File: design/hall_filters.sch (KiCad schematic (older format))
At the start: 11 parts

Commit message: Saved project with more recent version of KiCad. Added IRS2184 half bridge driver to BLDC_4_cache.lib
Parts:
- C4, C5, C6, C7: symbol C -> C-RESCUE-BLDC_4
- R10, R11, R12, R13, R7, R8, R9: symbol R -> R-RESCUE-BLDC_4
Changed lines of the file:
@@
 EESchema Schematic File Version 2
+LIBS:BLDC_4-rescue
 LIBS:power
 LIBS:device
@@
 LIBS:crf_1
 LIBS:BLDC_4-cache
-EELAYER 24 0
+EELAYER 25 0
 EELAYER END
 $Descr A4 11693 8268
@@
 $EndDescr
 $Comp
-L R R7
+L R-RESCUE-BLDC_4 R7
 U 1 1 53FBB581
 P 4900 3200
@@
 $EndComp
 $Comp
-L R R8
+L R-RESCUE-BLDC_4 R8
 U 1 1 53FBB588
 P 5550 3750
@@
 $EndComp
 $Comp
-L R R9
+L R-RESCUE-BLDC_4 R9
 U 1 1 53FBB58F
 P 5550 3650
@@
 $EndComp
 $Comp
-L R R10
+L R-RESCUE-BLDC_4 R10
 U 1 1 53FBB596
 P 5550 3550
@@
 $EndComp
 $Comp
-L C C5
+L C-RESCUE-BLDC_4 C5
 U 1 1 53FBB59D
 P 5950 4250
@@
 $EndComp
 $Comp
-L C C6
+L C-RESCUE-BLDC_4 C6
 U 1 1 53FBB5A4
 P 6200 4250
@@
 $EndComp
 $Comp
-L C C7
+L C-RESCUE-BLDC_4 C7
 U 1 1 53FBB5AB
 P 6450 4250
@@
 $EndComp
 $Comp
-L GND #PWR030
+L GND-RESCUE-BLDC_4 #PWR030
 U 1 1 53FBB5B2
 P 5950 4450
@@
 $EndComp
 $Comp
-L R R11
+L R-RESCUE-BLDC_4 R11
 U 1 1 53FBB5B8
 P 5000 3200
@@
 $EndComp
 $Comp
-L R R12
+L R-RESCUE-BLDC_4 R12
 U 1 1 53FBB5BF
 P 5100 3200
@@
 $EndComp
 $Comp
-L R R13
+L R-RESCUE-BLDC_4 R13
 U 1 1 53FBB5C6
 P 5200 3200
@@
 $EndComp
 $Comp
-L C C4
+L C-RESCUE-BLDC_4 C4
 U 1 1 53FBB5CD
 P 5100 4250
@@
 $EndComp
 $Comp
-L GND #PWR031
+L GND-RESCUE-BLDC_4 #PWR031
 U 1 1 53FBB5D4
 P 5100 4450
@@
 	5100 3850 5100 4050
 $Comp
-L GND #PWR033
+L GND-RESCUE-BLDC_4 #PWR033
 U 1 1 53FBB5F9
 P 6200 4450
@@
 $EndComp
 $Comp
-L GND #PWR034
+L GND-RESCUE-BLDC_4 #PWR034
 U 1 1 53FBB5FF
 P 6450 4450

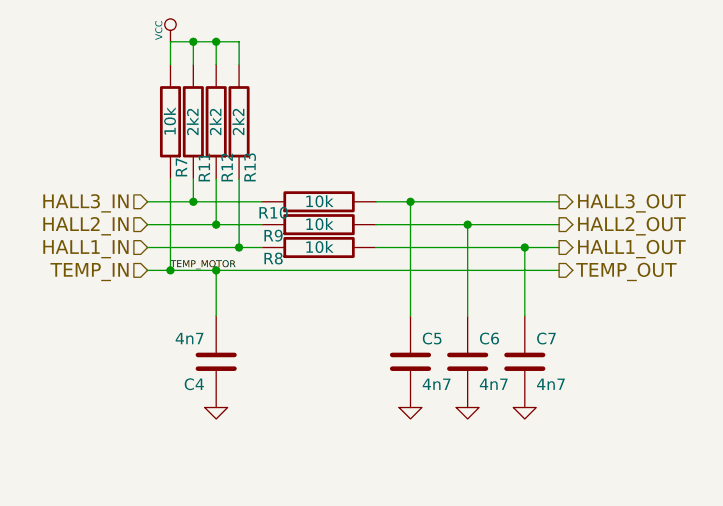
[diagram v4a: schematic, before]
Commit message: First complete draft of the schematics.
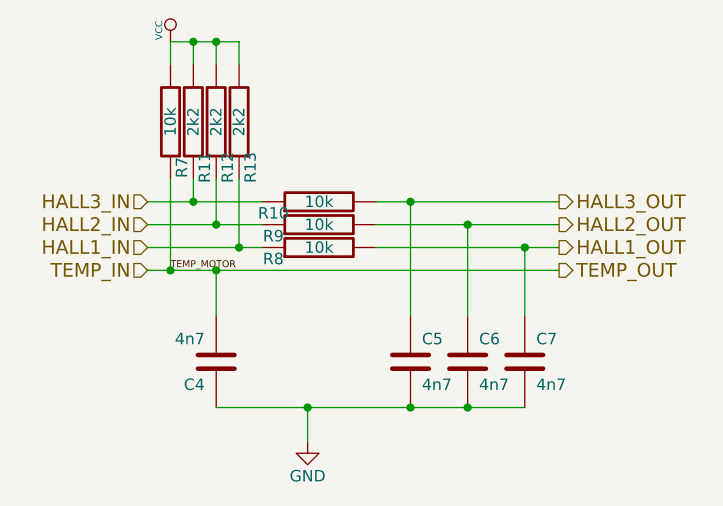
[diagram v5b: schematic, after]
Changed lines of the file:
@@
 $Descr A4 11693 8268
 encoding utf-8
-Sheet 4 10
+Sheet 4 11
 Title ""
-Date "25 Aug 2014"
+Date "2015-08-27"
 Rev ""
 Comp ""
@@
 $EndComp
 $Comp
-L GND-RESCUE-BLDC_4 #PWR030
-U 1 1 53FBB5B2
-P 5950 4450
-F 0 "#PWR030" H 5950 4450 30  0001 C CNN
-F 1 "GND" H 5950 4380 30  0001 C CNN
-F 2 "" H 5950 4450 60  0001 C CNN
-F 3 "" H 5950 4450 60  0001 C CNN
-	1    5950 4450
-	1    0    0    -1
-$EndComp
-$Comp
 L R-RESCUE-BLDC_4 R11
 U 1 1 53FBB5B8
@@
 $EndComp
 $Comp
-L GND-RESCUE-BLDC_4 #PWR031
-U 1 1 53FBB5D4
-P 5100 4450
-F 0 "#PWR031" H 5100 4450 30  0001 C CNN
-F 1 "GND" H 5100 4380 30  0001 C CNN
-F 2 "" H 5100 4450 60  0001 C CNN
-F 3 "" H 5100 4450 60  0001 C CNN
-	1    5100 4450
-	1    0    0    -1
-$EndComp
-$Comp
 L VCC #PWR032
 U 1 1 53FBB5DA
@@
 Wire Wire Line
 	5100 3850 5100 4050
-$Comp
-L GND-RESCUE-BLDC_4 #PWR033
-U 1 1 53FBB5F9
-P 6200 4450
-F 0 "#PWR033" H 6200 4450 30  0001 C CNN
-F 1 "GND" H 6200 4380 30  0001 C CNN
-F 2 "" H 6200 4450 60  0001 C CNN
-F 3 "" H 6200 4450 60  0001 C CNN
-	1    6200 4450
-	1    0    0    -1
-$EndComp
-$Comp
-L GND-RESCUE-BLDC_4 #PWR034
-U 1 1 53FBB5FF
-P 6450 4450
-F 0 "#PWR034" H 6450 4450 30  0001 C CNN
-F 1 "GND" H 6450 4380 30  0001 C CNN
-F 2 "" H 6450 4450 60  0001 C CNN
-F 3 "" H 6450 4450 60  0001 C CNN
-	1    6450 4450
-	1    0    0    -1
-$EndComp
 Text Label 4900 3850 0    30   ~ 0
 TEMP_MOTOR
@@
 Text HLabel 6600 3850 2    60   Output ~ 0
 TEMP_OUT
+$Comp
+L GND #PWR?
+U 1 1 55E74C47
+P 5500 4600
+F 0 "#PWR?" H 5500 4350 50  0001 C CNN
+F 1 "GND" H 5500 4450 50  0000 C CNN
+F 2 "" H 5500 4600 60  0000 C CNN
+F 3 "" H 5500 4600 60  0000 C CNN
+	1    5500 4600
+	1    0    0    -1
+$EndComp
+Wire Wire Line
+	5500 4600 5500 4450
+Wire Wire Line
+	5100 4450 6450 4450
+Connection ~ 5500 4450
+Connection ~ 5950 4450
+Connection ~ 6200 4450
 $EndSCHEMATC

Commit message: Assigned some footprints.
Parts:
- C4, C5, C6, C7: footprint SMD_Packages:SMD-0603_c -> Capacitors_SMD:C_0603
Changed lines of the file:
@@
 F 0 "C5" H 6000 4350 50  0000 L CNN
 F 1 "4n7" H 6000 4150 50  0000 L CNN
-F 2 "SMD_Packages:SMD-0603_c" H 5950 4250 60  0001 C CNN
+F 2 "Capacitors_SMD:C_0603" H 5950 4250 60  0001 C CNN
 F 3 "" H 5950 4250 60  0001 C CNN
 	1    5950 4250
@@
 F 0 "C6" H 6250 4350 50  0000 L CNN
 F 1 "4n7" H 6250 4150 50  0000 L CNN
-F 2 "SMD_Packages:SMD-0603_c" H 6200 4250 60  0001 C CNN
+F 2 "Capacitors_SMD:C_0603" H 6200 4250 60  0001 C CNN
 F 3 "" H 6200 4250 60  0001 C CNN
 	1    6200 4250
@@
 F 0 "C7" H 6500 4350 50  0000 L CNN
 F 1 "4n7" H 6500 4150 50  0000 L CNN
-F 2 "SMD_Packages:SMD-0603_c" H 6450 4250 60  0001 C CNN
+F 2 "Capacitors_SMD:C_0603" H 6450 4250 60  0001 C CNN
 F 3 "" H 6450 4250 60  0001 C CNN
 	1    6450 4250
@@
 F 0 "C4" H 5150 4350 50  0000 L CNN
 F 1 "4n7" H 5150 4150 50  0000 L CNN
-F 2 "SMD_Packages:SMD-0603_c" H 5100 4250 60  0001 C CNN
+F 2 "Capacitors_SMD:C_0603" H 5100 4250 60  0001 C CNN
 F 3 "" H 5100 4250 60  0001 C CNN
 	1    5100 4250
@@
 $EndComp
 $Comp
-L VCC #PWR032
+L VCC #PWR025
 U 1 1 53FBB5DA
 P 4900 2850
-F 0 "#PWR032" H 4900 2950 30  0001 C CNN
+F 0 "#PWR025" H 4900 2950 30  0001 C CNN
 F 1 "VCC" V 4850 2900 30  0000 C CNN
 F 2 "" H 4900 2850 60  0001 C CNN
@@
 TEMP_OUT
 $Comp
-L GND #PWR?
+L GND #PWR026
 U 1 1 55E74C47
 P 5500 4600
-F 0 "#PWR?" H 5500 4350 50  0001 C CNN
+F 0 "#PWR026" H 5500 4350 50  0001 C CNN
 F 1 "GND" H 5500 4450 50  0000 C CNN
 F 2 "" H 5500 4600 60  0000 C CNN

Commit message: Selected footprints
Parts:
- R10, R11, R12, R13, R7, R8, R9: footprint SMD_Packages:SMD-0603_r -> Resistors_SMD:R_0603
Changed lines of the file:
@@
 F 0 "R7" V 4850 3400 50  0000 C CNN
 F 1 "10k" V 4900 3200 50  0000 C CNN
-F 2 "SMD_Packages:SMD-0603_r" H 4900 3200 60  0001 C CNN
+F 2 "Resistors_SMD:R_0603" H 4900 3200 60  0001 C CNN
 F 3 "" H 4900 3200 60  0001 C CNN
 	1    4900 3200
@@
 F 0 "R8" V 5500 3950 50  0000 C CNN
 F 1 "10k" V 5550 3750 50  0000 C CNN
-F 2 "SMD_Packages:SMD-0603_r" H 5550 3750 60  0001 C CNN
+F 2 "Resistors_SMD:R_0603" H 5550 3750 60  0001 C CNN
 F 3 "" H 5550 3750 60  0001 C CNN
 	1    5550 3750
@@
 F 0 "R9" V 5500 3850 50  0000 C CNN
 F 1 "10k" V 5550 3650 50  0000 C CNN
-F 2 "SMD_Packages:SMD-0603_r" H 5550 3650 60  0001 C CNN
+F 2 "Resistors_SMD:R_0603" H 5550 3650 60  0001 C CNN
 F 3 "" H 5550 3650 60  0001 C CNN
 	1    5550 3650
@@
 F 0 "R10" V 5500 3750 50  0000 C CNN
 F 1 "10k" V 5550 3550 50  0000 C CNN
-F 2 "SMD_Packages:SMD-0603_r" H 5550 3550 60  0001 C CNN
+F 2 "Resistors_SMD:R_0603" H 5550 3550 60  0001 C CNN
 F 3 "" H 5550 3550 60  0001 C CNN
 	1    5550 3550
@@
 F 0 "R11" V 4950 3400 50  0000 C CNN
 F 1 "2k2" V 5000 3200 50  0000 C CNN
-F 2 "SMD_Packages:SMD-0603_r" H 5000 3200 60  0001 C CNN
+F 2 "Resistors_SMD:R_0603" H 5000 3200 60  0001 C CNN
 F 3 "" H 5000 3200 60  0001 C CNN
 	1    5000 3200
@@
 F 0 "R12" V 5050 3400 50  0000 C CNN
 F 1 "2k2" V 5100 3200 50  0000 C CNN
-F 2 "SMD_Packages:SMD-0603_r" H 5100 3200 60  0001 C CNN
+F 2 "Resistors_SMD:R_0603" H 5100 3200 60  0001 C CNN
 F 3 "" H 5100 3200 60  0001 C CNN
 	1    5100 3200
@@
 F 0 "R13" V 5150 3400 50  0000 C CNN
 F 1 "2k2" V 5200 3200 50  0000 C CNN
-F 2 "SMD_Packages:SMD-0603_r" H 5200 3200 60  0001 C CNN
+F 2 "Resistors_SMD:R_0603" H 5200 3200 60  0001 C CNN
 F 3 "" H 5200 3200 60  0001 C CNN
 	1    5200 3200
